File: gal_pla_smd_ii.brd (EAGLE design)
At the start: 18.3 x 37 mm, 4 parts

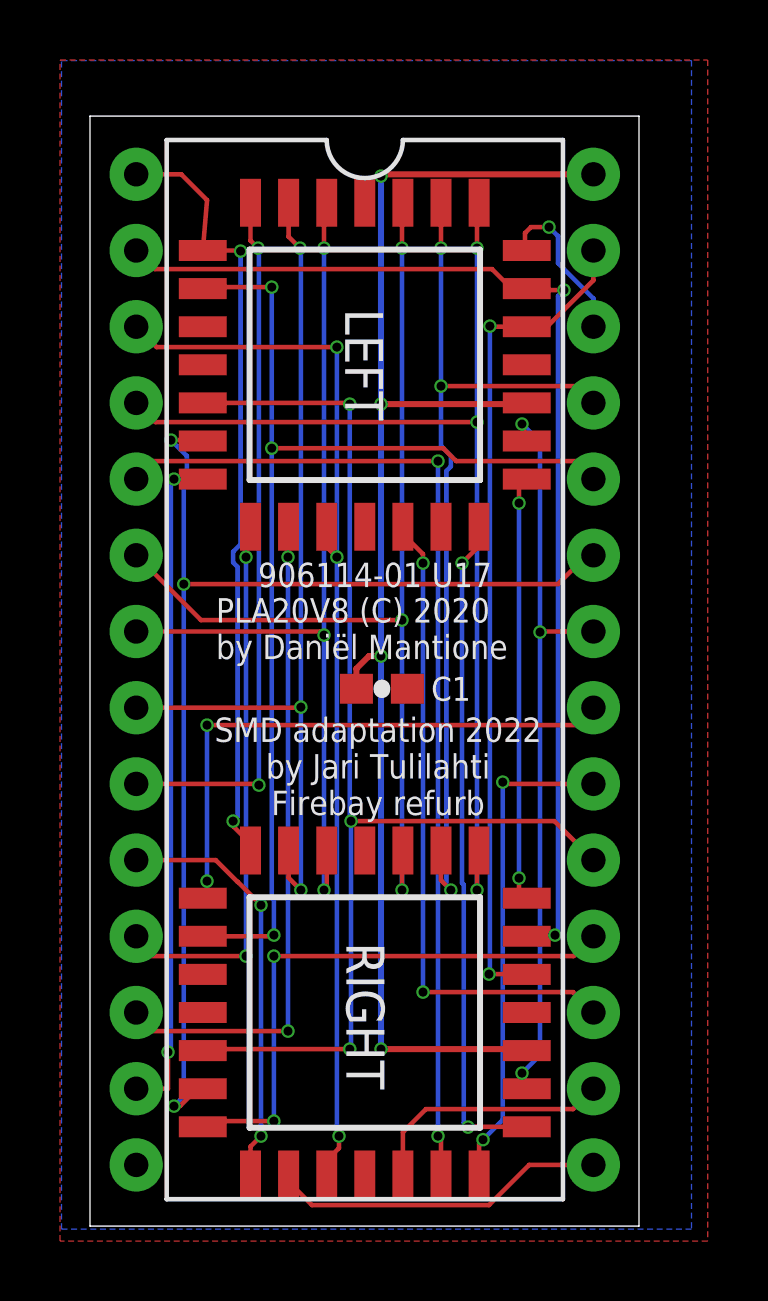
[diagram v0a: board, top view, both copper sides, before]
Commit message: Update to bigger pads for easier hand-soldering
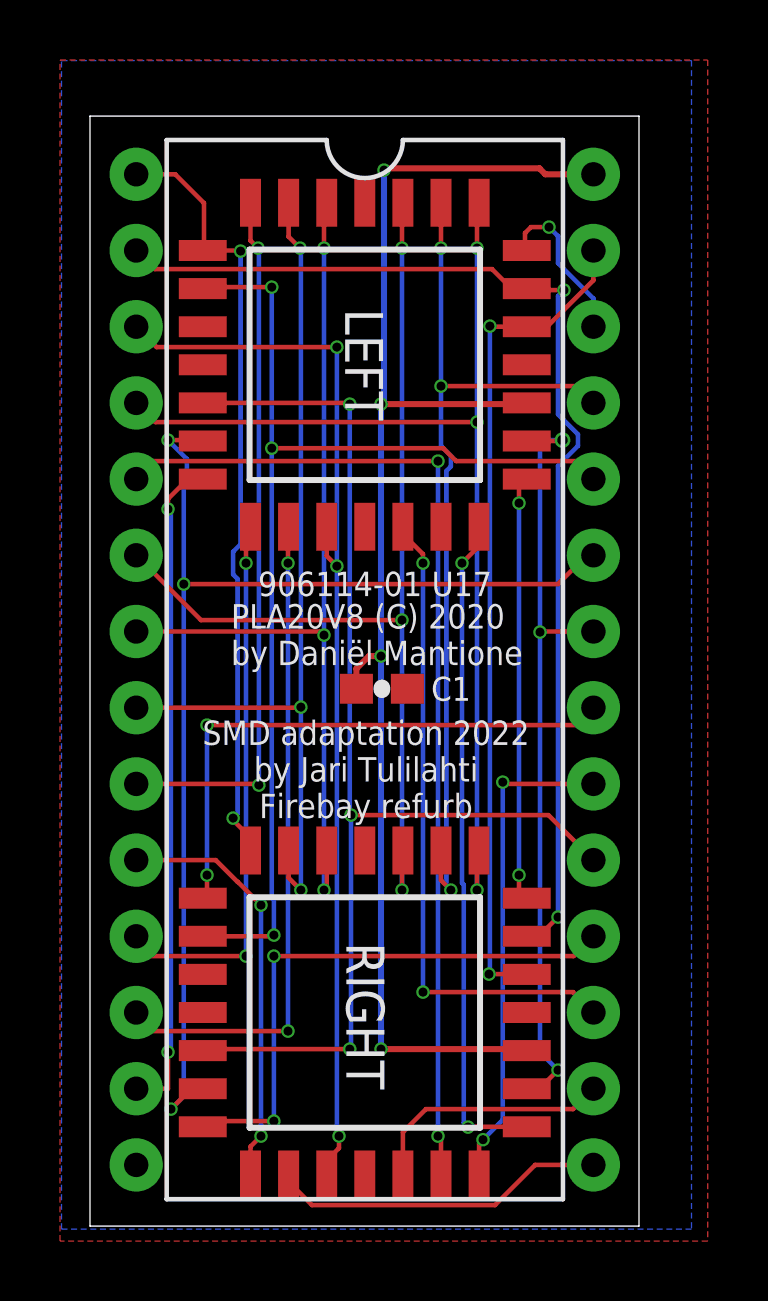
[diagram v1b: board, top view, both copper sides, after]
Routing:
- net I_GAME: track 25.1 -> 26.2 mm
